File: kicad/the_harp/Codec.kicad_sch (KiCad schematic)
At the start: 16 parts, among them IC501 AK4621EF, U501 OPA2348AIDR

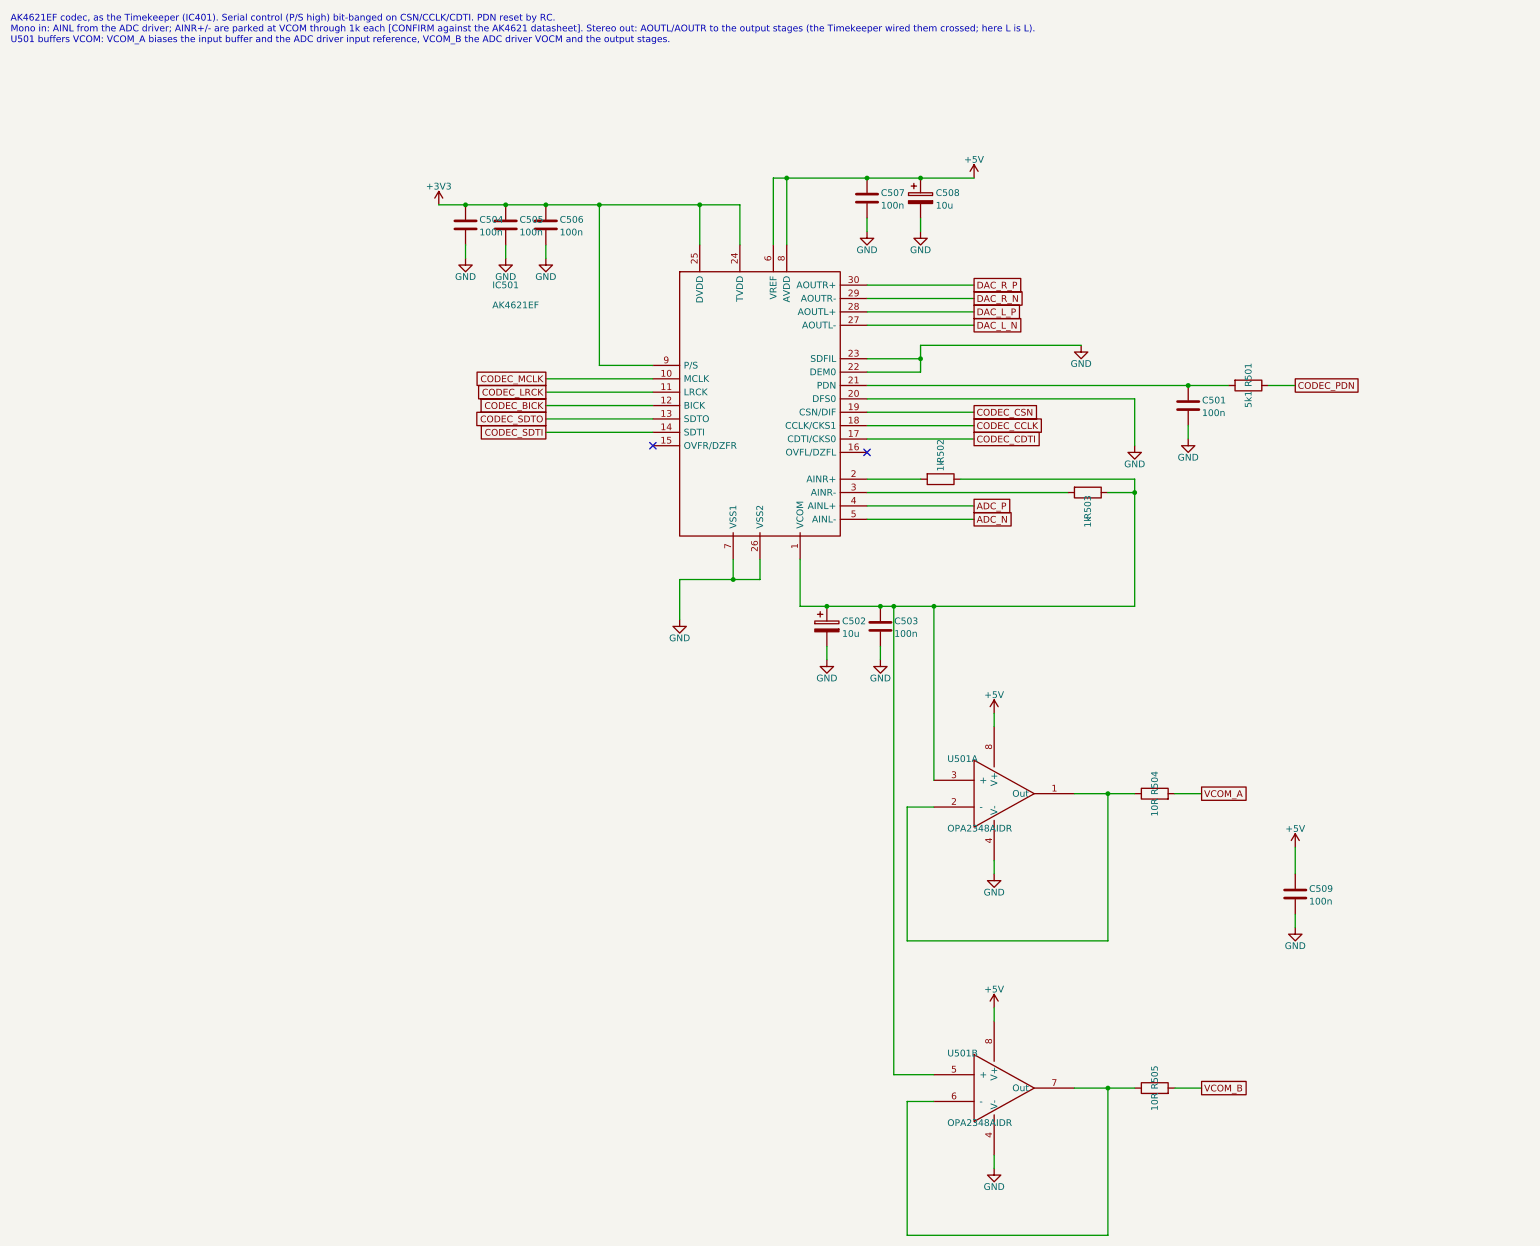
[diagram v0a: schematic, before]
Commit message: Stereo single-ended input and an OLED display
IN becomes a TRS jack (tip left, ring right) with a second OPA2365 buffer and
THS4522 channel B into the AK4621EF's AINR; the codec inputs are no longer
parked. A mono plug is detected by the right channel reading silence. The
twelve note LEDs and R107-R118 give way to a 0.91 in I2C OLED connector (J408,
PB6/PB7) with 4.7k pull-ups. Schematic regenerated (190 parts, netlist OK on
all sheets); design brief, PCB plan, firmware requirements and the design
report updated. The PCB still carries the old LED footprints until Update PCB
from Schematic is run in KiCad.

Co-Authored-By: Claude Sonnet 5.5 <noreply@anthropic.com>
Claude-Session: https://claude.ai/code/session_016hDejPHPgG8auBLMyByYZK
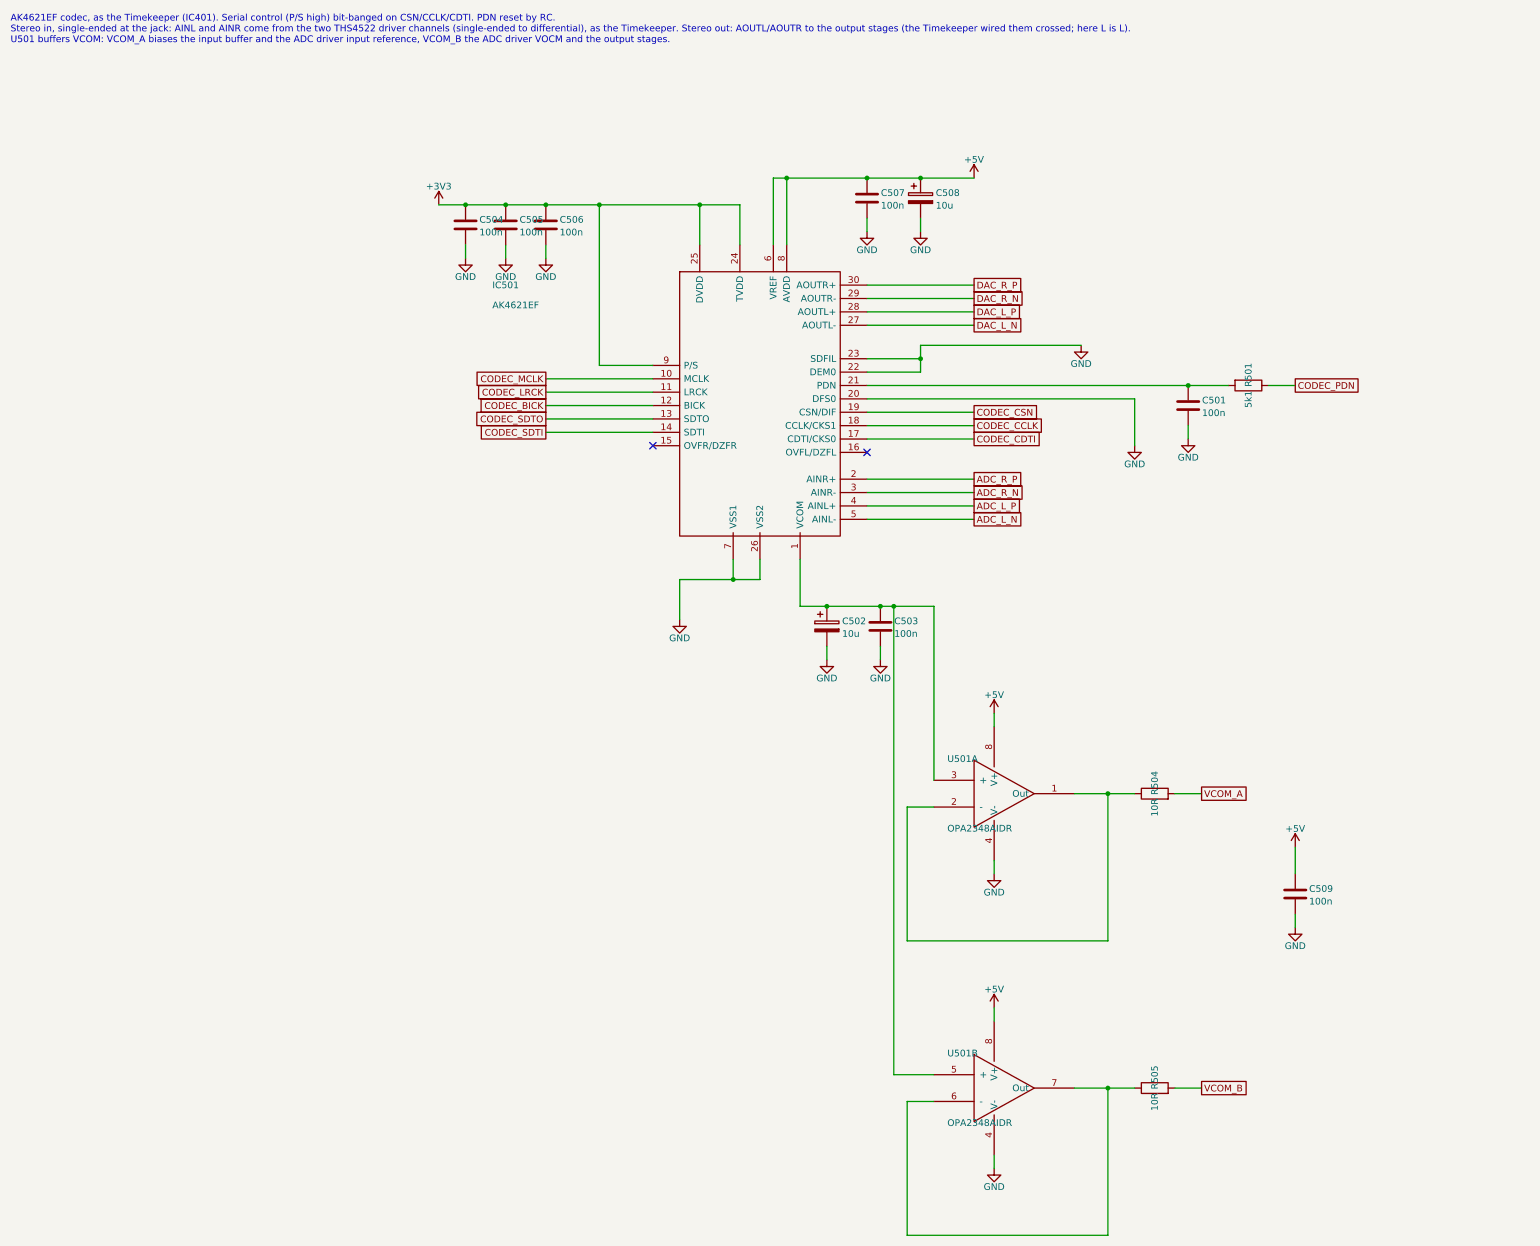
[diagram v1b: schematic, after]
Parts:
- removed R502, R503: 1k, Resistor_SMD:R_0603_1608Metric, symbol Device:R
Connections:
- net ADC_R_N: now reaches IC501.3 (AINR-)
- net ADC_R_P: now reaches IC501.2 (AINR+)
- net ADC_N renamed ADC_L_N
- net ADC_P renamed ADC_L_P
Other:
- note added: "AK4621EF codec, as the Timekeeper (IC401). Serial control (P/S high) bit-banged on CSN/CCLK/CDTI. PDN reset by RC. Stereo in, single-ended at the jack: AINL and AINR come from the two THS4522 driver channels (single-ended to differential), as the Timekeeper. Stereo out: AOUTL/AOUTR to the output stages (the Timekeeper wired them crossed; here L is L). U501 buffers VCOM: VCOM_A biases the input bu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"
- note removed: "AK4621EF codec, as the Timekeeper (IC401). Serial control (P/S high) bit-banged on CSN/CCLK/CDTI. PDN reset by RC. Mono in: AINL from the ADC driver; AINR+/- are parked at VCOM through 1k each [CONFIRM against the AK4621 datasheet]. Stereo out: AOUTL/AOUTR to the output stages (the Timekeeper wired them crossed; here L is L). U501 buffers VCOM: VCOM_A biases the input buffer and the ADC driver in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"
